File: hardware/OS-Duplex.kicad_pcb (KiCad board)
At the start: 2 copper layers, 46 x 37.5 mm, 46 parts, among them J201 Screw_Terminal_01x04, J3 ICSP, J62 Screw_Terminal_01x04, Q11 AO3400A, Q12 AO3400A, Q21 AO3400A, Q22 AO3400A, SW1 SW_SPST, SW901 SW_DIP_x05, U101 ATmega328-A, U301 AMS1117-5.0, U801 HCPL-0631, Y1 Crystal_GND2

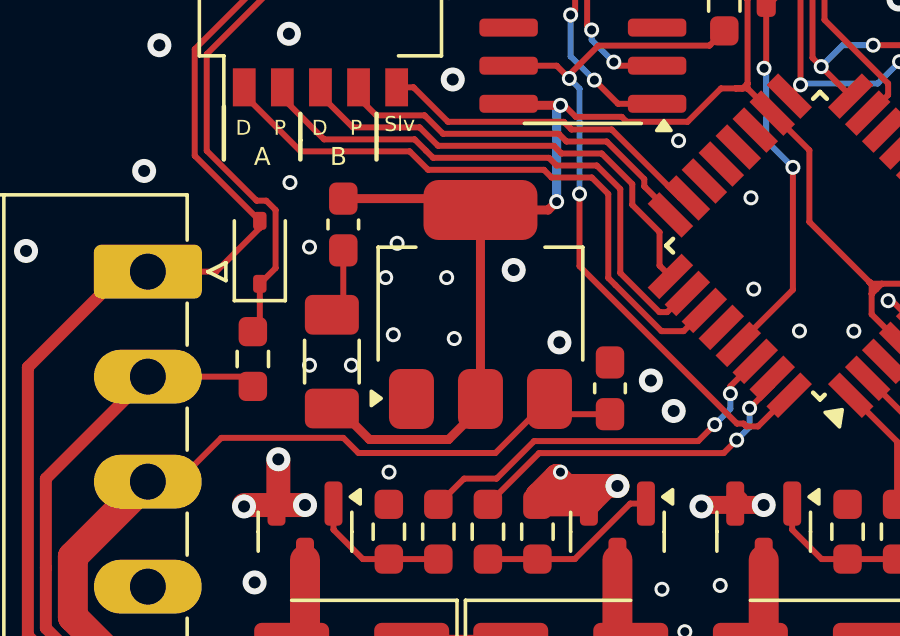
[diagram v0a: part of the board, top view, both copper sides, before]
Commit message: changed LDO
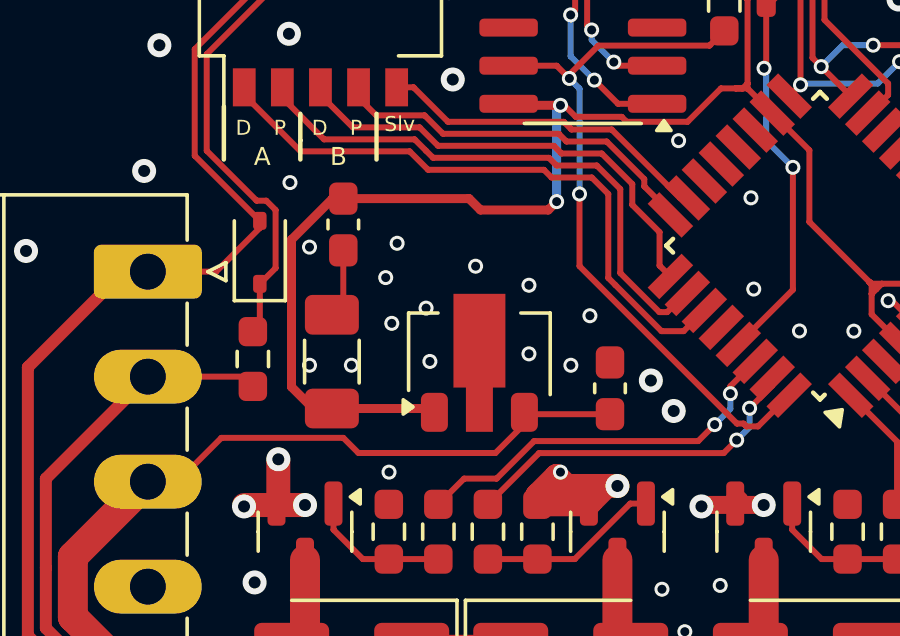
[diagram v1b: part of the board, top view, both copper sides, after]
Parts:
- removed U301: AMS1117-5.0, Package_TO_SOT_SMD:SOT-223-3_TabPin2
- added U21: L78L05_SOT89, Package_TO_SOT_SMD:SOT-89-3, F.Cu at (118.5, 73.2)
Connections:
- U101 pad 13: /atmega/GPIO1 -> unconnected-(U101-PB1-Pad13)
- U101 pad 14: /atmega/GPIO6 -> unconnected-(U101-PB2-Pad14)
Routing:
- net +5V: track 60.5 -> 61.5 mm
- net GND: vias 72 -> 75

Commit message: added translations
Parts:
- removed J201: Screw_Terminal_01x04, custom_kicad_lib_sk:connector_3.50mm_4P horizontal_MALE
- added J63: Screw_Terminal_01x04, Connector_Phoenix_MC:PhoenixContact_MC_1,5_4-G-3.5_1x04_P3.50mm_Horizontal, F.Cu at (144.0, 81.0)
- moved D4 1.58 mm to (143.0, 65.9)
- moved D2 1.58 mm to (143.0, 63.8)
- moved C302 1.32 mm to (114.8, 69.8), turned to 180 degrees
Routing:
- net GND: track 35.4 -> 38.9 mm, vias 75 -> 77
- net +5V: track 61.5 -> 62.2 mm
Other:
- board text added: "+ -"
- board text added: "12-18V"
- board text added: "D S"
- board text added: "DCC"
- board text added: "P C"
- board text removed: "D"
- board text removed: "P"
